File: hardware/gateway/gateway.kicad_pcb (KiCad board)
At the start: 2 copper layers, 100 x 45 mm, 79 parts, among them IC1 STM8L151K4T6, IC2 CC1101RGPR, IC3 LT1615ES5-1#TRMPBF, IC4 MIC4427YM, IC5 MB85RC64TAPNF-G-BDERE1, J1 G8250041000YEU, J2 M20-9770342, Q1 IRLML6402TRPBF, U1 2462, Y1 NX3225GA-26.000M-STD-CRG-2

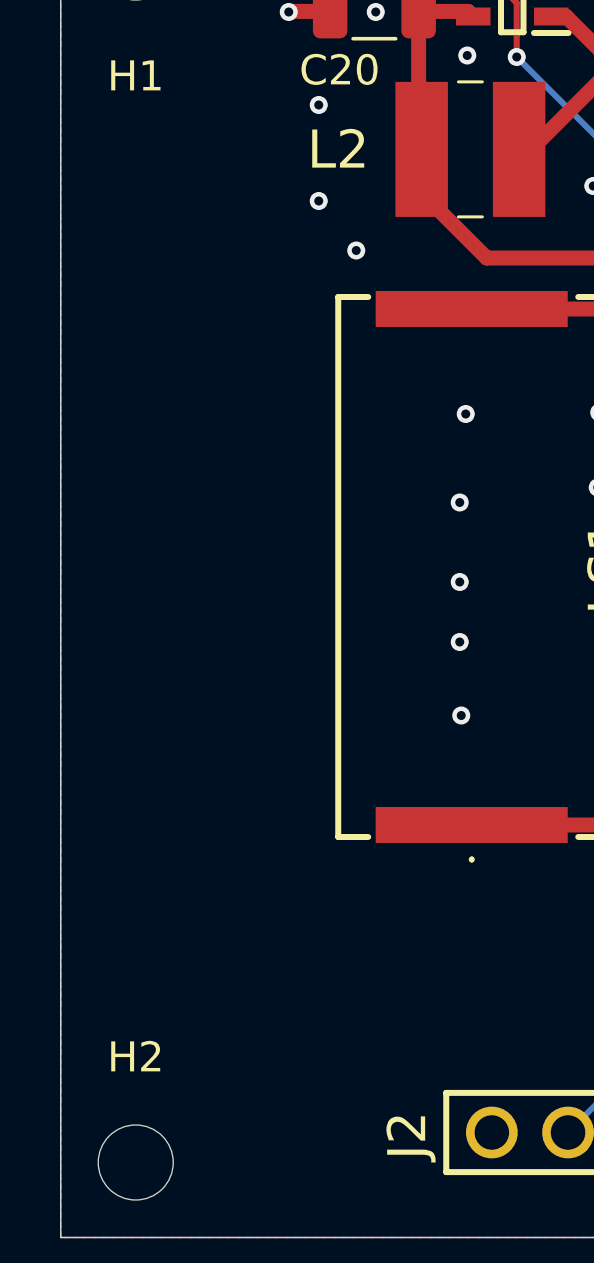
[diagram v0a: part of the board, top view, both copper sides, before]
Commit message: EG-33 Added the revision and name of the board on silkscreen.
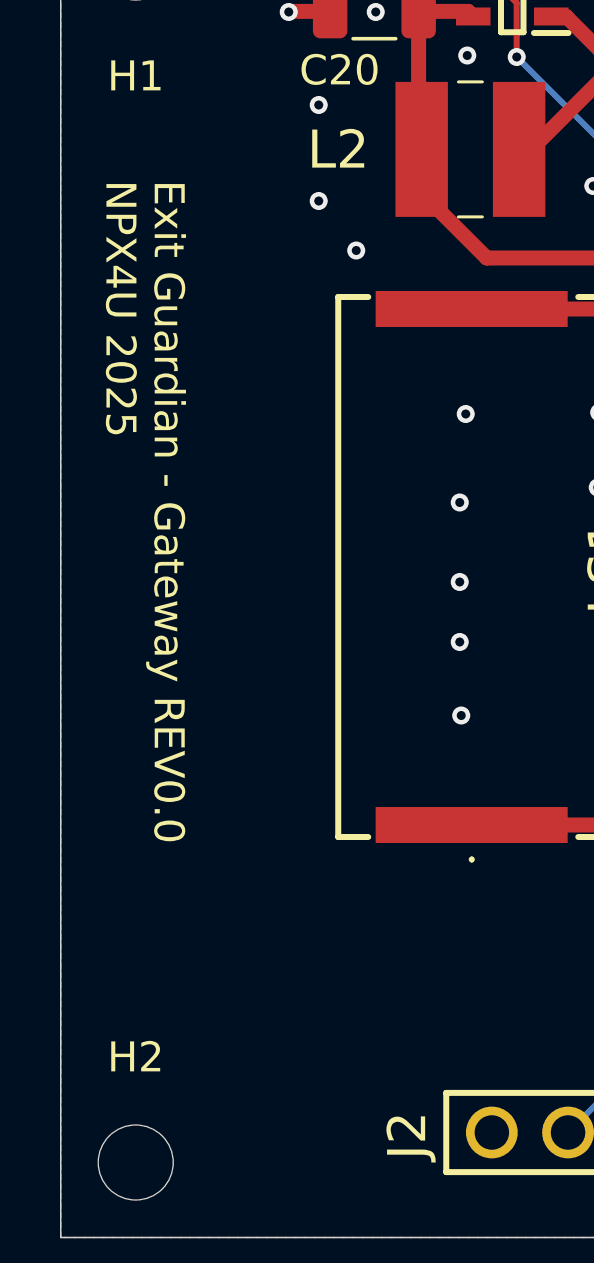
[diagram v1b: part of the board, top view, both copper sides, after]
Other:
- board text added: "Exit Guardian - Gateway REV0.0 NPX4U 2025"
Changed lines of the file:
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@@
 		(layer "Edge.Cuts")
+	)
+	(gr_text "Exit Guardian - Gateway REV0.0\nNPX4U 2025"
+		(at 180.9 124.7 270)
+		(layer "F.SilkS")
+		(effects
+			(font
+				(size 1 1)
+				(thickness 0.15)
+			)
+			(justify left bottom)
+		)
 	)
 	(segment
